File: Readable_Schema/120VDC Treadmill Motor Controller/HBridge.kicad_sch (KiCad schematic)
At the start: 75 parts, among them J2 OSTT7020150, Q1 IPP60R060P7XKSA1, Q2 IPP60R060P7XKSA1, Q3 IPP60R060P7XKSA1, Q4 IPP60R060P7XKSA1, U1 UCC21530DWKR, U2 UCC21530DWKR

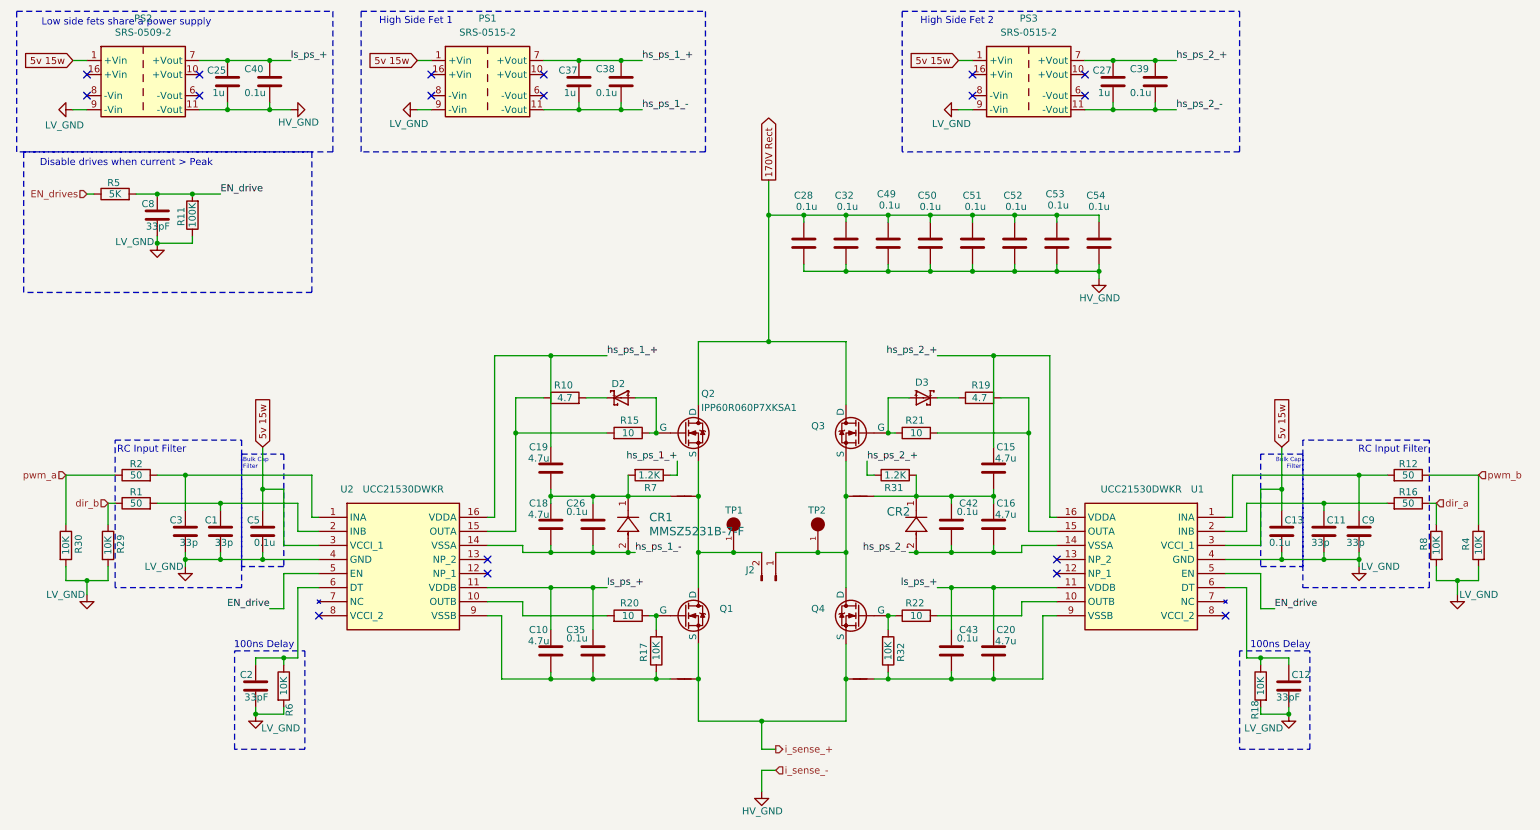
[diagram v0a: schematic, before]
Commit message: -Playing around with different layouts --With the additional two layers the GND and 5V planes can be shared amongst all LV components, making things a bit easier and pushing me to really start laying a bunch of SMD components one on top of the other.
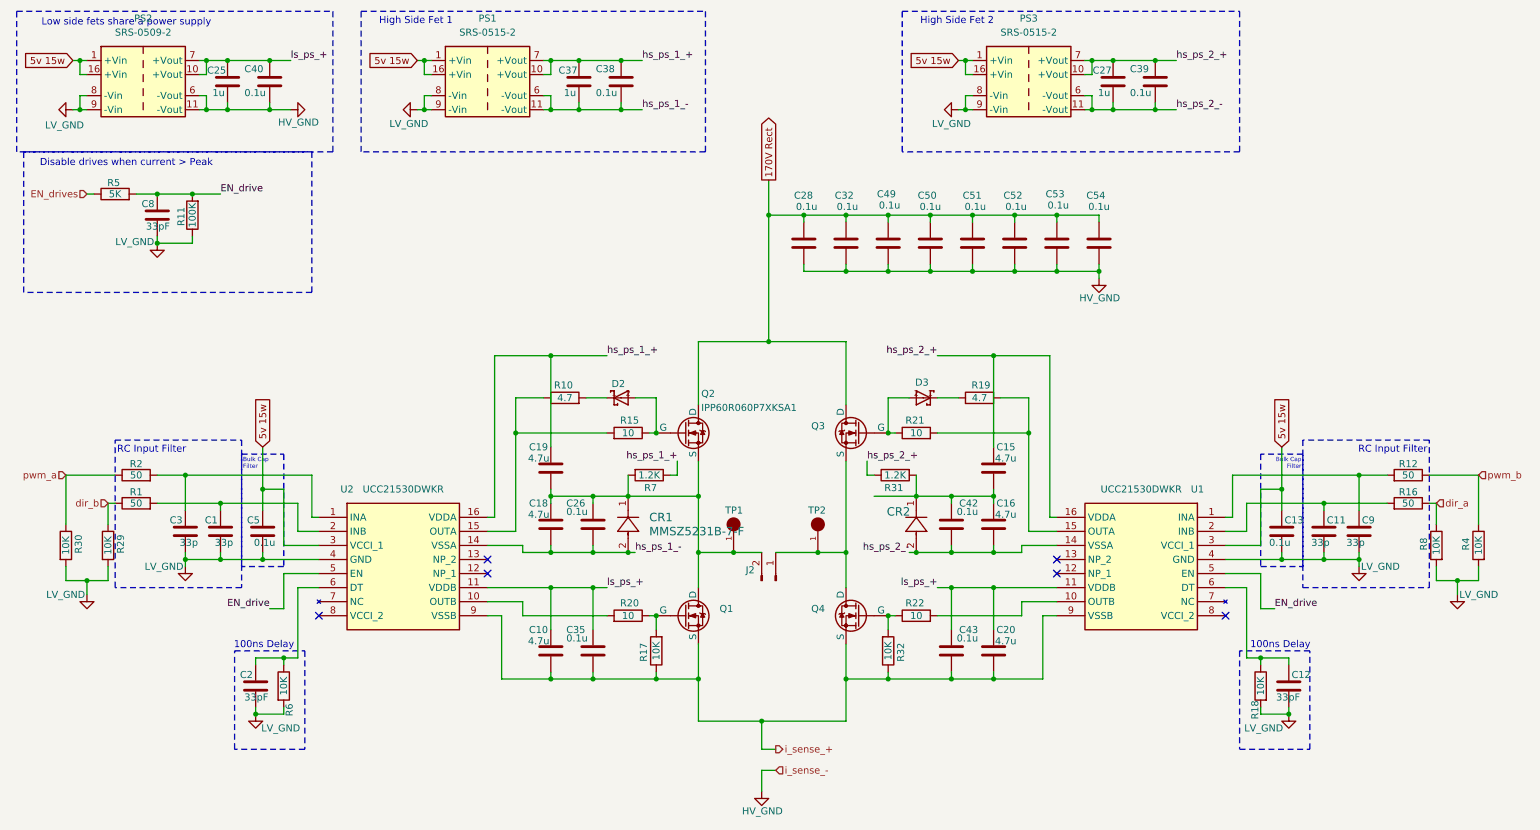
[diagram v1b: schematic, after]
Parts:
- removed NT1, NT2, NT3, NT4: NetTie_2, NetTie:NetTie-2_THT_Pad0.3mm, symbol Device:NetTie_2
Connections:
- net 5v 15w: now also PS1.16 (+Vin), PS2.16 (+Vin), PS3.16 (+Vin)
- net HV_GND: now also PS2.6 (-Vout)
- net LV_GND: now also PS1.8 (-Vin), PS2.8 (-Vin), PS3.8 (-Vin)
- net hs_ps_1_+: now also PS1.10 (+Vout)
- net hs_ps_1_-: now also PS1.6 (-Vout)
- net hs_ps_2_+: now also PS3.10 (+Vout)
- net hs_ps_2_-: now also PS3.6 (-Vout)
- net i_sense_+: now also C10.2, C20.2, C35.2, C43.2, R17.1, R32.1, U1.9 (VSSB), U2.9 (VSSB)
- net ls_ps_+: now also PS2.10 (+Vout)
- net at C18.1, C19.2, C26.1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: now also J2.2 (Pin_2), Q1.2 (D), Q2.3 (S), TP1.1
- no-connect marks 18 -> 6

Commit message: -Changed all footprints from metric to imperial sizing --This meant repositioning everything on the board again.
-Did the first pour for HV GND
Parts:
- C1, C10, C11, C12, C13, C15, C16, C18, C19, C2, C20, C26, C3, C35, C38, C39, C40, C42, C43, C5, C8, C9: footprint Capacitor_SMD:C_0201_0603Metric_Pad0.64x0.40mm_HandSolder -> Capacitor_SMD:C_0603_1608Metric_Pad1.08x0.95mm_HandSolder
- C25, C27, C37: footprint Capacitor_SMD:C_0402_1005Metric_Pad0.74x0.62mm_HandSolder -> Capacitor_SMD:C_1206_3216Metric_Pad1.33x1.80mm_HandSolder
- R1, R11, R12, R16, R17, R18, R2, R29, R30, R31, R32, R4, R5, R6, R7, R8: footprint Resistor_SMD:R_0201_0603Metric_Pad0.64x0.40mm_HandSolder -> Resistor_SMD:R_0603_1608Metric_Pad0.98x0.95mm_HandSolder
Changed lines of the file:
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@@
 			)
 		)
-		(property "Footprint" "Capacitor_SMD:C_0201_0603Metric_Pad0.64x0.40mm_HandSolder"
+		(property "Footprint" "Capacitor_SMD:C_0603_1608Metric_Pad1.08x0.95mm_HandSolder"
 			(at 242.2652 138.43 0)
 			(effects
@@
 			)
 		)
-		(property "Footprint" "Capacitor_SMD:C_0201_0603Metric_Pad0.64x0.40mm_HandSolder"
+		(property "Footprint" "Capacitor_SMD:C_0603_1608Metric_Pad1.08x0.95mm_HandSolder"
 			(at 116.5352 132.08 0)
 			(effects
@@
 			)
 		)
-		(property "Footprint" "Capacitor_SMD:C_0201_0603Metric_Pad0.64x0.40mm_HandSolder"
+		(property "Footprint" "Capacitor_SMD:C_0603_1608Metric_Pad1.08x0.95mm_HandSolder"
 			(at 188.9252 109.22 0)
 			(effects
@@
 			)
 		)
-		(property "Footprint" "Resistor_SMD:R_0201_0603Metric_Pad0.64x0.40mm_HandSolder"
+		(property "Footprint" "Resistor_SMD:R_0603_1608Metric_Pad0.98x0.95mm_HandSolder"
 			(at 44.958 49.53 90)
 			(effects
@@
 			)
 		)
-		(property "Footprint" "Capacitor_SMD:C_0201_0603Metric_Pad0.64x0.40mm_HandSolder"
+		(property "Footprint" "Capacitor_SMD:C_0603_1608Metric_Pad1.08x0.95mm_HandSolder"
 			(at 254.9652 110.49 0)
 			(effects
@@
 			)
 		)
-		(property "Footprint" "Resistor_SMD:R_0201_0603Metric_Pad0.64x0.40mm_HandSolder"
+		(property "Footprint" "Resistor_SMD:R_0603_1608Metric_Pad0.98x0.95mm_HandSolder"
 			(at 262.89 103.378 90)
 			(effects
@@
 			)
 		)
-		(property "Footprint" "Capacitor_SMD:C_0201_0603Metric_Pad0.64x0.40mm_HandSolder"
+		(property "Footprint" "Capacitor_SMD:C_0603_1608Metric_Pad1.08x0.95mm_HandSolder"
 			(at 188.9252 132.08 0)
 			(effects
@@
 			)
 		)
-		(property "Footprint" "Resistor_SMD:R_0201_0603Metric_Pad0.64x0.40mm_HandSolder"
+		(property "Footprint" "Resistor_SMD:R_0603_1608Metric_Pad0.98x0.95mm_HandSolder"
 			(at 29.21 47.498 90)
 			(effects
@@
 			)
 		)
-		(property "Footprint" "Resistor_SMD:R_0201_0603Metric_Pad0.64x0.40mm_HandSolder"
+		(property "Footprint" "Resistor_SMD:R_0603_1608Metric_Pad0.98x0.95mm_HandSolder"
 			(at 125.73 94.742 90)
 			(effects
@@
 			)
 		)
-		(property "Footprint" "Resistor_SMD:R_0201_0603Metric_Pad0.64x0.40mm_HandSolder"
+		(property "Footprint" "Resistor_SMD:R_0603_1608Metric_Pad0.98x0.95mm_HandSolder"
 			(at 237.998 134.62 90)
 			(effects
@@
 			)
 		)
-		(property "Footprint" "Capacitor_SMD:C_0201_0603Metric_Pad0.64x0.40mm_HandSolder"
+		(property "Footprint" "Capacitor_SMD:C_0603_1608Metric_Pad1.08x0.95mm_HandSolder"
 			(at 40.9448 110.49 0)
 			(effects
@@
 			)
 		)
-		(property "Footprint" "Capacitor_SMD:C_0201_0603Metric_Pad0.64x0.40mm_HandSolder"
+		(property "Footprint" "Capacitor_SMD:C_0603_1608Metric_Pad1.08x0.95mm_HandSolder"
 			(at 106.9848 132.08 0)
 			(effects
@@
 			)
 		)
-		(property "Footprint" "Resistor_SMD:R_0201_0603Metric_Pad0.64x0.40mm_HandSolder"
+		(property "Footprint" "Resistor_SMD:R_0603_1608Metric_Pad0.98x0.95mm_HandSolder"
 			(at 277.368 109.22 90)
 			(effects
@@
 			)
 		)
-		(property "Footprint" "Capacitor_SMD:C_0201_0603Metric_Pad0.64x0.40mm_HandSolder"
+		(property "Footprint" "Capacitor_SMD:C_0603_1608Metric_Pad1.08x0.95mm_HandSolder"
 			(at 58.1152 29.21 0)
 			(effects
@@
 			)
 		)
-		(property "Footprint" "Capacitor_SMD:C_0201_0603Metric_Pad0.64x0.40mm_HandSolder"
+		(property "Footprint" "Capacitor_SMD:C_0603_1608Metric_Pad1.08x0.95mm_HandSolder"
 			(at 106.9848 109.22 0)
 			(effects
@@
 			)
 		)
-		(property "Footprint" "Resistor_SMD:R_0201_0603Metric_Pad0.64x0.40mm_HandSolder"
+		(property "Footprint" "Resistor_SMD:R_0603_1608Metric_Pad0.98x0.95mm_HandSolder"
 			(at 269.748 109.22 90)
 			(effects
@@
 			)
 		)
-		(property "Footprint" "Capacitor_SMD:C_0402_1005Metric_Pad0.74x0.62mm_HandSolder"
+		(property "Footprint" "Capacitor_SMD:C_1206_3216Metric_Pad1.33x1.80mm_HandSolder"
 			(at 208.5848 29.21 0)
 			(effects
@@
 			)
 		)
-		(property "Footprint" "Capacitor_SMD:C_0201_0603Metric_Pad0.64x0.40mm_HandSolder"
+		(property "Footprint" "Capacitor_SMD:C_0603_1608Metric_Pad1.08x0.95mm_HandSolder"
 			(at 179.3748 109.22 0)
 			(effects
@@
 			)
 		)
-		(property "Footprint" "Resistor_SMD:R_0201_0603Metric_Pad0.64x0.40mm_HandSolder"
+		(property "Footprint" "Resistor_SMD:R_0603_1608Metric_Pad0.98x0.95mm_HandSolder"
 			(at 170.18 94.742 90)
 			(effects
@@
 			)
 		)
-		(property "Footprint" "Capacitor_SMD:C_0201_0603Metric_Pad0.64x0.40mm_HandSolder"
+		(property "Footprint" "Capacitor_SMD:C_0603_1608Metric_Pad1.08x0.95mm_HandSolder"
 			(at 179.3748 132.08 0)
 			(effects
@@
 			)
 		)
-		(property "Footprint" "Resistor_SMD:R_0201_0603Metric_Pad0.64x0.40mm_HandSolder"
+		(property "Footprint" "Resistor_SMD:R_0603_1608Metric_Pad0.98x0.95mm_HandSolder"
 			(at 33.02 103.378 90)
 			(effects
@@
 			)
 		)
-		(property "Footprint" "Capacitor_SMD:C_0402_1005Metric_Pad0.74x0.62mm_HandSolder"
+		(property "Footprint" "Capacitor_SMD:C_1206_3216Metric_Pad1.33x1.80mm_HandSolder"
 			(at 112.0648 29.21 0)
 			(effects
@@
 			)
 		)
-		(property "Footprint" "Resistor_SMD:R_0201_0603Metric_Pad0.64x0.40mm_HandSolder"
+		(property "Footprint" "Resistor_SMD:R_0603_1608Metric_Pad0.98x0.95mm_HandSolder"
 			(at 33.02 98.298 90)
 			(effects
@@
 			)
 		)
-		(property "Footprint" "Capacitor_SMD:C_0201_0603Metric_Pad0.64x0.40mm_HandSolder"
+		(property "Footprint" "Capacitor_SMD:C_0603_1608Metric_Pad1.08x0.95mm_HandSolder"
 			(at 47.2948 110.49 0)
 			(effects
@@
 			)
 		)
-		(property "Footprint" "Capacitor_SMD:C_0201_0603Metric_Pad0.64x0.40mm_HandSolder"
+		(property "Footprint" "Capacitor_SMD:C_0603_1608Metric_Pad1.08x0.95mm_HandSolder"
 			(at 188.9252 99.06 0)
 			(effects
@@
 			)
 		)
-		(property "Footprint" "Capacitor_SMD:C_0201_0603Metric_Pad0.64x0.40mm_HandSolder"
+		(property "Footprint" "Capacitor_SMD:C_0603_1608Metric_Pad1.08x0.95mm_HandSolder"
 			(at 248.6152 110.49 0)
 			(effects
@@
 			)
 		)
-		(property "Footprint" "Capacitor_SMD:C_0201_0603Metric_Pad0.64x0.40mm_HandSolder"
+		(property "Footprint" "Capacitor_SMD:C_0603_1608Metric_Pad1.08x0.95mm_HandSolder"
 			(at 121.6152 29.21 0)
 			(effects
@@
 			)
 		)
-		(property "Footprint" "Capacitor_SMD:C_0201_0603Metric_Pad0.64x0.40mm_HandSolder"
+		(property "Footprint" "Capacitor_SMD:C_0603_1608Metric_Pad1.08x0.95mm_HandSolder"
 			(at 35.8648 53.34 0)
 			(effects
@@
 			)
 		)
-		(property "Footprint" "Capacitor_SMD:C_0201_0603Metric_Pad0.64x0.40mm_HandSolder"
+		(property "Footprint" "Capacitor_SMD:C_0603_1608Metric_Pad1.08x0.95mm_HandSolder"
 			(at 54.9148 110.49 0)
 			(effects
@@
 			)
 		)
-		(property "Footprint" "Resistor_SMD:R_0201_0603Metric_Pad0.64x0.40mm_HandSolder"
+		(property "Footprint" "Resistor_SMD:R_0603_1608Metric_Pad0.98x0.95mm_HandSolder"
 			(at 18.542 109.22 90)
 			(effects
@@
 			)
 		)
-		(property "Footprint" "Resistor_SMD:R_0201_0603Metric_Pad0.64x0.40mm_HandSolder"
+		(property "Footprint" "Resistor_SMD:R_0603_1608Metric_Pad0.98x0.95mm_HandSolder"
 			(at 262.89 98.298 90)
 			(effects
@@
 			)
 		)
-		(property "Footprint" "Resistor_SMD:R_0201_0603Metric_Pad0.64x0.40mm_HandSolder"
+		(property "Footprint" "Resistor_SMD:R_0603_1608Metric_Pad0.98x0.95mm_HandSolder"
 			(at 128.778 128.27 90)
 			(effects
@@
 			)
 		)
-		(property "Footprint" "Capacitor_SMD:C_0402_1005Metric_Pad0.74x0.62mm_HandSolder"
+		(property "Footprint" "Capacitor_SMD:C_1206_3216Metric_Pad1.33x1.80mm_HandSolder"
 			(at 48.5648 29.21 0)
 			(effects
@@
 			)
 		)
-		(property "Footprint" "Capacitor_SMD:C_0201_0603Metric_Pad0.64x0.40mm_HandSolder"
+		(property "Footprint" "Capacitor_SMD:C_0603_1608Metric_Pad1.08x0.95mm_HandSolder"
 			(at 240.9952 110.49 0)
 			(effects
@@
 			)
 		)
-		(property "Footprint" "Resistor_SMD:R_0201_0603Metric_Pad0.64x0.40mm_HandSolder"
+		(property "Footprint" "Resistor_SMD:R_0603_1608Metric_Pad0.98x0.95mm_HandSolder"
 			(at 57.912 134.62 90)
 			(effects
@@
 			)
 		)
-		(property "Footprint" "Capacitor_SMD:C_0201_0603Metric_Pad0.64x0.40mm_HandSolder"
+		(property "Footprint" "Capacitor_SMD:C_0603_1608Metric_Pad1.08x0.95mm_HandSolder"
 			(at 53.6448 138.43 0)
 			(effects
@@
 			)
 		)
-		(property "Footprint" "Capacitor_SMD:C_0201_0603Metric_Pad0.64x0.40mm_HandSolder"
+		(property "Footprint" "Capacitor_SMD:C_0603_1608Metric_Pad1.08x0.95mm_HandSolder"
 			(at 116.5352 109.22 0)
 			(effects
@@
 			)
 		)
-		(property "Footprint" "Capacitor_SMD:C_0201_0603Metric_Pad0.64x0.40mm_HandSolder"
+		(property "Footprint" "Capacitor_SMD:C_0603_1608Metric_Pad1.08x0.95mm_HandSolder"
 			(at 106.9848 99.06 0)
 			(effects
@@
 			)
 		)
-		(property "Footprint" "Capacitor_SMD:C_0201_0603Metric_Pad0.64x0.40mm_HandSolder"
+		(property "Footprint" "Capacitor_SMD:C_0603_1608Metric_Pad1.08x0.95mm_HandSolder"
 			(at 218.1352 29.21 0)
 			(effects
@@
 			)
 		)
-		(property "Footprint" "Resistor_SMD:R_0201_0603Metric_Pad0.64x0.40mm_HandSolder"
+		(property "Footprint" "Resistor_SMD:R_0603_1608Metric_Pad0.98x0.95mm_HandSolder"
 			(at 26.162 109.22 90)
 			(effects
@@
 			)
 		)
-		(property "Footprint" "Resistor_SMD:R_0201_0603Metric_Pad0.64x0.40mm_HandSolder"
+		(property "Footprint" "Resistor_SMD:R_0603_1608Metric_Pad0.98x0.95mm_HandSolder"
 			(at 167.132 128.27 90)
 			(effects

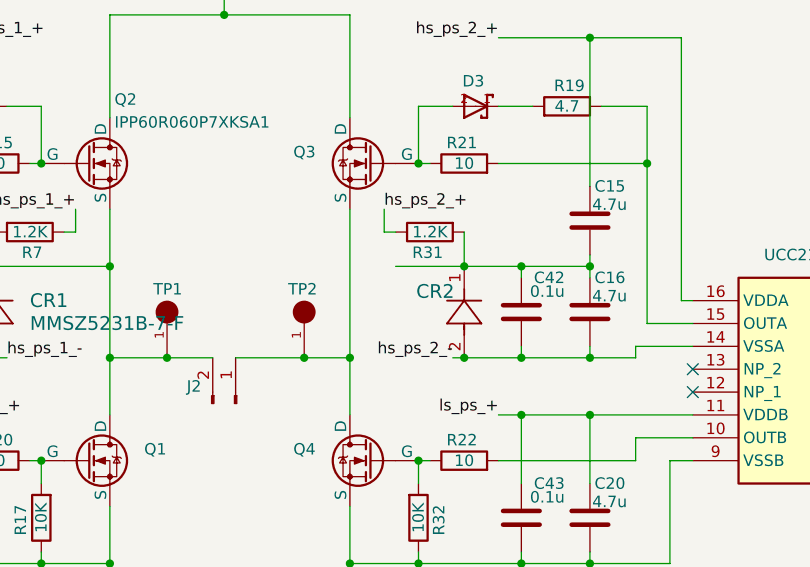
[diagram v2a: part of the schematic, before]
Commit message: Added a few more fill zones for high power stuff
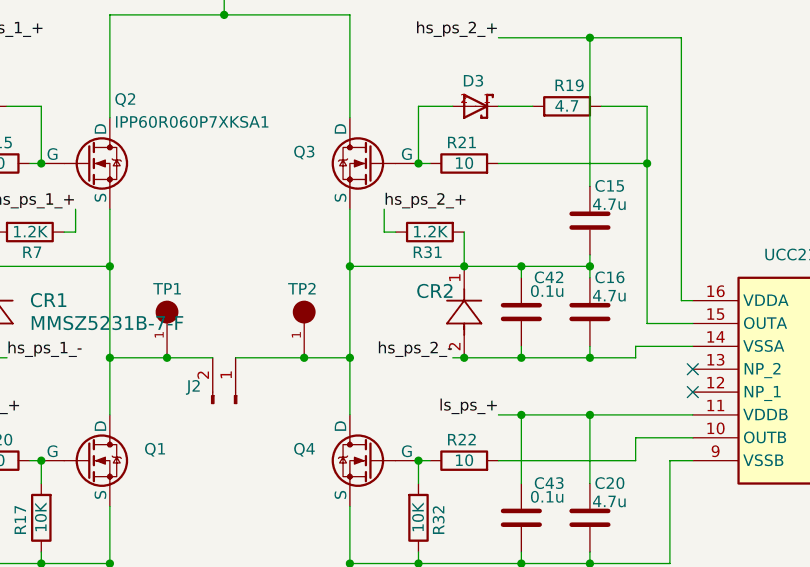
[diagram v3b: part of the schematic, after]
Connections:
- net at C15.2, C16.1, C42.1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: now also J2.1 (Pin_1), Q3.3 (S), Q4.2 (D), TP2.1
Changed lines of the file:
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@@
+	)
+	(junction
+		(at 161.29 100.33)
+		(diameter 0)
+		(color 0 0 0 0)
 	)
 	(junction
@@
 	(wire
 		(pts
+			(xy 161.29 100.33) (xy 161.29 110.49)
+		)
+		(stroke
+			(width 0)
+			(type default)
+		)
+	)
+	(wire
+		(pts
 			(xy 180.34 109.22) (xy 180.34 110.49)
 		)
@@
 	(wire
 		(pts
+			(xy 161.29 100.33) (xy 173.99 100.33)
+		)
+		(stroke
+			(width 0)
+			(type default)
+		)
+	)
+	(wire
+		(pts
 			(xy 115.57 109.22) (xy 115.57 110.49)
 		)
@@
 	(wire
 		(pts
-			(xy 161.29 93.98) (xy 161.29 110.49)
+			(xy 161.29 93.98) (xy 161.29 100.33)
 		)
 		(stroke
@@
 		)
 		(stroke
-			(width 0)
-			(type default)
-		)
-	)
-	(wire
-		(pts
-			(xy 173.99 100.33) (xy 166.37 100.33)
-		)
-		(stroke

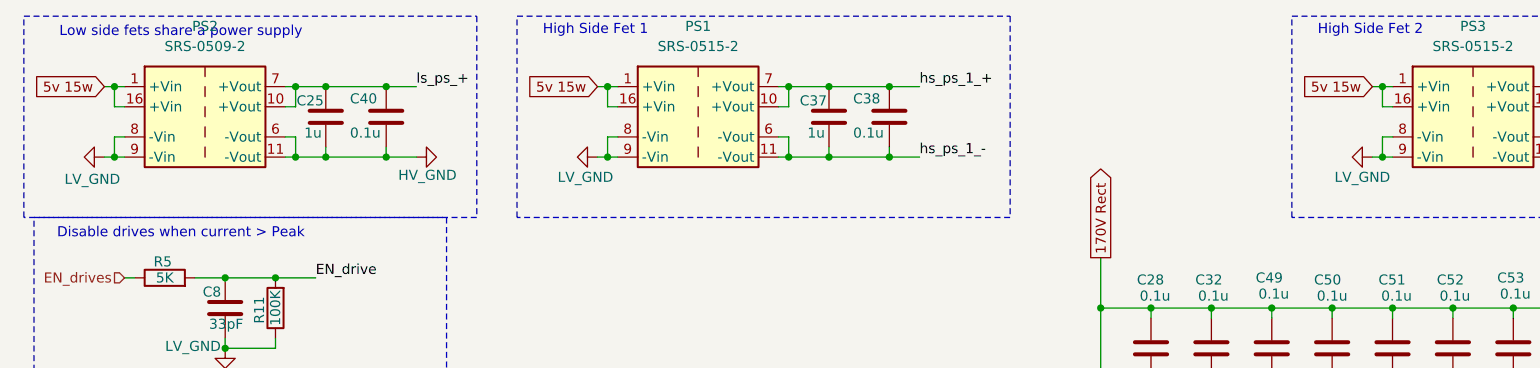
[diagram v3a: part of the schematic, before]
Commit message: Almost done connecting all the traces on the H bridge side, Sounding like Pete is going to bash on this pretty hard so will likely need to redo all this. Good practice regardless
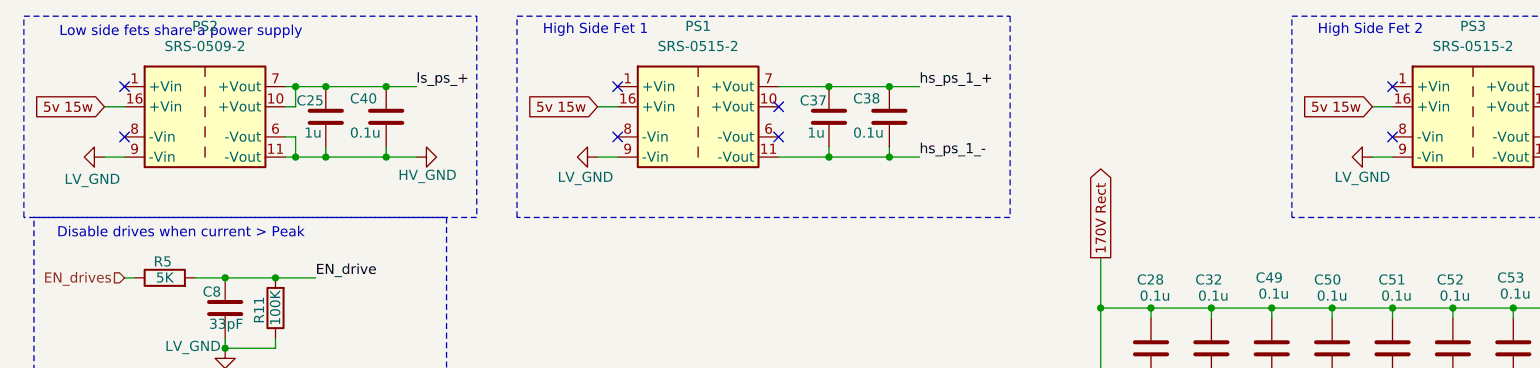
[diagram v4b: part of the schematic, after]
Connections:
- net 5v 15w: no longer PS1.1 (+Vin), PS2.1 (+Vin), PS3.1 (+Vin)
- net LV_GND: no longer PS1.8 (-Vin), PS2.8 (-Vin), PS3.8 (-Vin)
- net hs_ps_1_+: no longer PS1.10 (+Vout)
- net hs_ps_1_-: no longer PS1.6 (-Vout)
- no-connect marks 6 -> 14
